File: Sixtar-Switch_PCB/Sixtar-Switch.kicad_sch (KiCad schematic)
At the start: 0 parts

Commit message: 닌텐도 스위치의 모든 버튼 및 axis 작동 확인 - GPIO0 ~ 13 = 스위치 버튼 Y, B, A, X, L트리거, R트리거, ZL트리거, ZR트리거, 마이너스, 플러스, L스틱, R스틱, 홈, 캡쳐 - GPIO14 = L스틱 왼쪽방향으로 틀기 - GPIO15 = R스틱 오른쪽방향으로 틀기
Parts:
- added K1, K10, K11, K12, K13, K14, K15, K16, K2, K3, K4, K5, K6, K7, K8, K9: KEYSW, symbol keyboard_parts:KEYSW

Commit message: kicad 회로 수정
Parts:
- added DPad_Down(GPIO17), DPad_Left(GPIO18), DPad_Right(GPIO19), DPad_Up(GPIO16): KEYSW, symbol keyboard_parts:KEYSW
- added J1: USB_C_Receptacle, symbol Connector:USB_C_Receptacle
- added R0, R1, R10, R11, R12, R13, R14, R15, R16, R17, R18, R19, R2, R3, R4, R5, R6, R7, R8, R9: 4.7k, symbol Device:R
- renumbered K10 to BT_+(GPIO9), K9 to BT_-(GPIO8), K3 to BT_A(GPIO2), K2 to BT_B(GPIO1), K14 to BT_Capture(GPIO13), K13 to BT_Home(GPIO12), K5 to BT_L(GPIO4), K11 to BT_LS(GPIO10), K15 to BT_LXAxis(GPIO14), K6 to BT_R(GPIO5), K12 to BT_RS(GPIO11), K16 to BT_RXAxis(GPIO15), K4 to BT_X(GPIO3), K1 to BT_Y(GPIO0), K7 to BT_ZL(GPIO6), K8 to BT_ZR(GPIO7)
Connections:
- net at BT_ZR(GPIO7).2: now also R7.2
- net at BT_LS(GPIO10).2: now also R10.2
- net at BT_Home(GPIO12).2: now also R12.2
- net at BT_RS(GPIO11).2: now also R11.2
- net at BT_R(GPIO5).2: now also R5.2
- net at BT_Y(GPIO0).2: now also R0.2
- net at BT_LXAxis(GPIO14).2: now also R14.2
- net at BT_Capture(GPIO13).2: now also R13.2
- net at BT_ZL(GPIO6).2: now also R6.2
- net at BT_B(GPIO1).2: now also R1.2
- net at BT_L(GPIO4).2: now also R4.2
- net at BT_A(GPIO2).2: now also R2.2
- net at BT_-(GPIO8).2: now also R8.2
- net at BT_RXAxis(GPIO15).2: now also R15.2
- net at BT_+(GPIO9).2: now also R9.2
- net at BT_X(GPIO3).2: now also R3.2
- new net: DPad_Up(GPIO16).2, R16.2
- new net: DPad_Down(GPIO17).2, R17.2
- new net: DPad_Left(GPIO18).2, R18.2
- new net: J1.A1 (GND), J1.A12 (GND), J1.B1 (GND), J1.B12 (GND)
- new net: J1.A4 (VBUS), J1.A9 (VBUS), J1.B4 (VBUS), J1.B9 (VBUS)
- new net: DPad_Right(GPIO19).2, R19.2
- no-connect marks 0 -> 10
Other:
- moved on the sheet: BT_+(GPIO9), BT_-(GPIO8), BT_A(GPIO2), BT_B(GPIO1), BT_Capture(GPIO13), BT_Home(GPIO12), BT_L(GPIO4), BT_LS(GPIO10), BT_LXAxis(GPIO14), BT_R(GPIO5), BT_RS(GPIO11), BT_RXAxis(GPIO15)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

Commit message: kicad 회로 수정
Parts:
- removed R0: 4.7k, symbol Device:R
- added C1, C2, C3: 10u, Capacitor_SMD:C_0805_2012Metric_Pad1.18x1.45mm_HandSolder, symbol Device:C
- added C10, C11, C12, C13, C5, C6, C7, C8, C9: 100u, Capacitor_SMD:C_0805_2012Metric_Pad1.18x1.45mm_HandSolder, symbol Device:C
- added C14, C15: 1u, Capacitor_SMD:C_0805_2012Metric_Pad1.18x1.45mm_HandSolder, symbol Device:C
- added C16, C17: 27p, Capacitor_SMD:C_0805_2012Metric_Pad1.18x1.45mm_HandSolder, symbol Device:C
- added C4: 100n, Capacitor_SMD:C_0805_2012Metric_Pad1.18x1.45mm_HandSolder, symbol Device:C
- added R10, R20, R9: 1k, Resistor_SMD:R_0805_2012Metric_Pad1.20x1.40mm_HandSolder, symbol Device:R
- added R2, R3: 5.1k, Resistor_SMD:R_0805_2012Metric_Pad1.20x1.40mm_HandSolder, symbol Device:R
- added R27: 4.7k, Resistor_SMD:R_0805_2012Metric_Pad1.20x1.40mm_HandSolder, symbol Device:R
- added R5, R6: 22, Resistor_SMD:R_0805_2012Metric_Pad1.20x1.40mm_HandSolder, symbol Device:R
- added SW1: USB_Boot, Connector_PinSocket_2.54mm:PinSocket_1x02_P2.54mm_Vertical, symbol Switch:SW_Push
- added SW2: RUN, Connector_PinSocket_2.54mm:PinSocket_1x02_P2.54mm_Vertical, symbol Switch:SW_Push
- added TP1, TP2: TestPoint, TestPoint:TestPoint_Pad_4.0x4.0mm, symbol Connector:TestPoint
- added U1: AMS1117-3.3, Package_TO_SOT_SMD:SOT-223-3_TabPin2, symbol Regulator_Linear:AMS1117-3.3
- added U2: W25Q128JVS, Package_SO:SOIC-8_5.23x5.23mm_P1.27mm, symbol Memory_Flash:W25Q128JVS
- added U3: RP2040, Package_DFN_QFN:QFN-56-1EP_7x7mm_P0.4mm_EP3.2x3.2mm, symbol MCU_RaspberryPi:RP2040
- added Y1: 12.000MHz(ATS,SMD), Crystal:Crystal_SMD_5032-2Pin_5.0x3.2mm, symbol Device:Crystal
- BT_+(GPIO9)1: renamed from BT_+(GPIO9); footprint (none) -> Button_Switch_Keyboard:SW_Cherry_MX_1.00u_PCB
- BT_-(GPIO8)1: renamed from BT_-(GPIO8); footprint (none) -> Button_Switch_Keyboard:SW_Cherry_MX_1.00u_PCB
- BT_A(GPIO2)1: renamed from BT_A(GPIO2); footprint (none) -> Button_Switch_Keyboard:SW_Cherry_MX_1.00u_PCB
- BT_B(GPIO1)1: renamed from BT_B(GPIO1); footprint (none) -> Button_Switch_Keyboard:SW_Cherry_MX_1.00u_PCB
- BT_Capture(GPIO13)1: renamed from BT_Capture(GPIO13); footprint (none) -> Button_Switch_Keyboard:SW_Cherry_MX_1.00u_PCB
- BT_Home(GPIO12)1: renamed from BT_Home(GPIO12); footprint (none) -> Button_Switch_Keyboard:SW_Cherry_MX_1.00u_PCB
- BT_L(GPIO4)1: renamed from BT_L(GPIO4); footprint (none) -> Button_Switch_Keyboard:SW_Cherry_MX_1.00u_PCB
- BT_LS(GPIO10)1: renamed from BT_LS(GPIO10); footprint (none) -> Button_Switch_Keyboard:SW_Cherry_MX_1.00u_PCB
- BT_LXAxis(GPIO14)1: renamed from BT_LXAxis(GPIO14); footprint (none) -> Button_Switch_Keyboard:SW_Cherry_MX_2.00u_PCB
- BT_R(GPIO5)1: renamed from BT_R(GPIO5); footprint (none) -> Button_Switch_Keyboard:SW_Cherry_MX_1.00u_PCB
- BT_RS(GPIO11)1: renamed from BT_RS(GPIO11); footprint (none) -> Button_Switch_Keyboard:SW_Cherry_MX_1.00u_PCB
- BT_RXAxis(GPIO15)1: renamed from BT_RXAxis(GPIO15); footprint (none) -> Button_Switch_Keyboard:SW_Cherry_MX_2.00u_PCB
- BT_X(GPIO3)1: renamed from BT_X(GPIO3); footprint (none) -> Button_Switch_Keyboard:SW_Cherry_MX_1.00u_PCB
- BT_Y(GPIO0)1: renamed from BT_Y(GPIO0); footprint (none) -> Button_Switch_Keyboard:SW_Cherry_MX_1.00u_PCB
- BT_ZL(GPIO6)1: renamed from BT_ZL(GPIO6); footprint (none) -> Button_Switch_Keyboard:SW_Cherry_MX_2.00u_PCB
- BT_ZR(GPIO7)1: renamed from BT_ZR(GPIO7); footprint (none) -> Button_Switch_Keyboard:SW_Cherry_MX_2.00u_PCB
- DPad_Down(GPIO17)1: renamed from DPad_Down(GPIO17); footprint (none) -> Button_Switch_Keyboard:SW_Cherry_MX_1.00u_PCB
- DPad_Left(GPIO18)1: renamed from DPad_Left(GPIO18); footprint (none) -> Button_Switch_Keyboard:SW_Cherry_MX_1.00u_PCB
- DPad_Right(GPIO19)1: renamed from DPad_Right(GPIO19); footprint (none) -> Button_Switch_Keyboard:SW_Cherry_MX_1.00u_PCB
- DPad_Up(GPIO16)1: renamed from DPad_Up(GPIO16); footprint (none) -> Button_Switch_Keyboard:SW_Cherry_MX_1.00u_PCB
- J1: footprint (none) -> Connector_USB:USB_C_Receptacle_XKB_U262-16XN-4BVC11
- R1: footprint (none) -> Resistor_SMD:R_0805_2012Metric_Pad1.20x1.40mm_HandSolder
- R11: renamed from R5; footprint (none) -> Resistor_SMD:R_0805_2012Metric_Pad1.20x1.40mm_HandSolder
- R12: renamed from R6; footprint (none) -> Resistor_SMD:R_0805_2012Metric_Pad1.20x1.40mm_HandSolder
- R13: renamed from R7; footprint (none) -> Resistor_SMD:R_0805_2012Metric_Pad1.20x1.40mm_HandSolder
- R14: renamed from R8; footprint (none) -> Resistor_SMD:R_0805_2012Metric_Pad1.20x1.40mm_HandSolder
- R15: renamed from R9; footprint (none) -> Resistor_SMD:R_0805_2012Metric_Pad1.20x1.40mm_HandSolder
- R16: renamed from R10; footprint (none) -> Resistor_SMD:R_0805_2012Metric_Pad1.20x1.40mm_HandSolder
- R17: renamed from R11; footprint (none) -> Resistor_SMD:R_0805_2012Metric_Pad1.20x1.40mm_HandSolder
- R18: renamed from R12; footprint (none) -> Resistor_SMD:R_0805_2012Metric_Pad1.20x1.40mm_HandSolder
- R19: renamed from R13; footprint (none) -> Resistor_SMD:R_0805_2012Metric_Pad1.20x1.40mm_HandSolder
- R21: renamed from R14; footprint (none) -> Resistor_SMD:R_0805_2012Metric_Pad1.20x1.40mm_HandSolder
- R22: renamed from R15; footprint (none) -> Resistor_SMD:R_0805_2012Metric_Pad1.20x1.40mm_HandSolder
- R23: renamed from R16; footprint (none) -> Resistor_SMD:R_0805_2012Metric_Pad1.20x1.40mm_HandSolder
- R24: renamed from R17; footprint (none) -> Resistor_SMD:R_0805_2012Metric_Pad1.20x1.40mm_HandSolder
- R25: renamed from R18; footprint (none) -> Resistor_SMD:R_0805_2012Metric_Pad1.20x1.40mm_HandSolder
- R26: renamed from R19; footprint (none) -> Resistor_SMD:R_0805_2012Metric_Pad1.20x1.40mm_HandSolder
- R4: renamed from R2; footprint (none) -> Resistor_SMD:R_0805_2012Metric_Pad1.20x1.40mm_HandSolder
- R7: renamed from R3; footprint (none) -> Resistor_SMD:R_0805_2012Metric_Pad1.20x1.40mm_HandSolder
- R8: renamed from R4; footprint (none) -> Resistor_SMD:R_0805_2012Metric_Pad1.20x1.40mm_HandSolder
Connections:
- net GND: now reaches BT_ZR(GPIO7)1.1
- net GND: now also BT_+(GPIO9)1.1, BT_-(GPIO8)1.1, BT_A(GPIO2)1.1, BT_B(GPIO1)1.1, BT_Capture(GPIO13)1.1, BT_Home(GPIO12)1.1, BT_L(GPIO4)1.1, BT_LS(GPIO10)1.1, BT_LXAxis(GPIO14)1.1, BT_R(GPIO5)1.1, BT_RS(GPIO11)1.1, BT_RXAxis(GPIO15)1.1, BT_X(GPIO3)1.1, BT_Y(GPIO0)1.1, BT_ZL(GPIO6)1.1, DPad_Down(GPIO17)1.1, DPad_Left(GPIO18)1.1, DPad_Right(GPIO19)1.1, DPad_Up(GPIO16)1.1, J1.A1 (GND), J1.A12 (GND), J1.B1 (GND), J1.B12 (GND), C1.1, C10.2, C11.2, C12.2, C13.2, C14.2, C15.2, C16.1, C17.1, C2.1, C3.1, C4.2, C5.2, C6.2, C7.2, C8.2, C9.2, R2.2, R3.2, SW1.1, SW2.1, U1.1 (GND), U2.4 (GND), U3.19 (TESTEN), U3.57 (GND)
- net BTN_ZL: now reaches R13.2
- net BTN_ZL: now also BT_ZL(GPIO6)1.2, U3.8 (GPIO6); no longer BT_ZR(GPIO7)1.2
- net +3.3V: now reaches R11.1
- net +3.3V: now also R1.1, R12.1, R13.1, R14.1, R15.1, R16.1, R17.1, R18.1, R19.1, R21.1, R22.1, R23.1, R24.1, R25.1, R26.1, R4.1, R7.1, R8.1, C10.1, C11.1, C12.1, C13.1, C15.1, C2.2, C3.2, C4.1, C7.1, C8.1, C9.1, R27.1, R9.2, U1.2 (VO), U2.8 (VCC), U3.1 (IOVDD), U3.10 (IOVDD), U3.22 (IOVDD), U3.33 (IOVDD), U3.42 (IOVDD), U3.43 (ADC_AVDD), U3.44 (VREG_IN), U3.48 (USB_VDD), U3.49 (IOVDD)
- net BTN_L: now reaches R11.2
- net BTN_L: now also BT_L(GPIO4)1.2, U3.6 (GPIO4); no longer BT_R(GPIO5)1.2
- net BTN_RXAxis: now reaches R23.2
- net BTN_RXAxis: now also BT_RXAxis(GPIO15)1.2, U3.18 (GPIO15); no longer DPad_Up(GPIO16)1.2
- net BTN_Capture: now reaches BT_Capture(GPIO13)1.2
- net BTN_Capture: now also R21.2, U3.16 (GPIO13); no longer R19.2
- net DPad_Down: now reaches DPad_Down(GPIO17)1.2
- net DPad_Down: now also R25.2, U3.28 (GPIO17); no longer R24.2
- net BTN_LS: now reaches BT_LS(GPIO10)1.2
- net BTN_LS: now also R17.2, U3.13 (GPIO10); no longer R16.2
- net BTN_B: now reaches BT_B(GPIO1)1.2
- net BTN_B: now also R4.2, U3.3 (GPIO1); no longer R1.2
- net BTN_Home: now reaches BT_Home(GPIO12)1.2
- net BTN_Home: now also R19.2, U3.15 (GPIO12); no longer R18.2
- net BTN_RS: now reaches BT_RS(GPIO11)1.2
- net BTN_RS: now also R18.2, U3.14 (GPIO11); no longer R17.2
- net DPad_Left: now reaches DPad_Left(GPIO18)1.2
- net DPad_Left: now also R26.2, U3.29 (GPIO18); no longer R25.2
- net BTN_Y: now reaches BT_Y(GPIO0)1.2
- net BTN_Y: now also R1.2, U3.2 (GPIO0)
- net BTN_LXAxis: now reaches BT_LXAxis(GPIO14)1.2
- net BTN_LXAxis: now also R22.2, U3.17 (GPIO14); no longer R21.2
- net BTN_Minus: now reaches R15.2
- net BTN_Minus: now also BT_-(GPIO8)1.2, U3.11 (GPIO8); no longer BT_+(GPIO9)1.2
- net BTN_R: now reaches R12.2
- net BTN_R: now also BT_R(GPIO5)1.2, U3.7 (GPIO5); no longer BT_ZL(GPIO6)1.2
- net VBUS: now reaches J1.A4 (VBUS), J1.A9 (VBUS), J1.B4 (VBUS), J1.B9 (VBUS)
- net VBUS: now also C1.2, U1.3 (VI)
- net at J1.A5 (CC1): now also R2.1
- net D+: now reaches J1.A6 (D+)
- net D+: now also J1.B6 (D+), R6.1
- net D-: now reaches J1.A7 (D-)
- net D-: now also J1.B7 (D-), R5.1
- net at J1.B5 (CC2): now also R3.1
- net GNDPWR: now reaches J1.S1 (SHIELD)
- net BTN_X: now reaches R8.2
- net BTN_X: now also BT_X(GPIO3)1.2, U3.5 (GPIO3); no longer BT_L(GPIO4)1.2
- net BTN_A: now reaches BT_A(GPIO2)1.2
- net BTN_A: now also R7.2, U3.4 (GPIO2); no longer R4.2
- net BTN_ZR: now reaches R14.2
- net BTN_ZR: now also BT_ZR(GPIO7)1.2, U3.9 (GPIO7); no longer BT_-(GPIO8)1.2
- net DPad_Right: now reaches DPad_Right(GPIO19)1.2
- net DPad_Right: now also R27.2, U3.30 (GPIO19); no longer R26.2
- new net: C17.2, R20.1, Y1.1
- new net: C16.2, U3.20 (XIN), Y1.2
- new net: R20.2, U3.21 (XOUT)
- new net: TP1.1, U3.24 (SWCLK)
- new net: TP2.1, U3.25 (SWD)
- new net: SW2.2, U3.26 (RUN)
- new net: R10.1, SW1.2
- new net +1V1: C14.1, C5.1, C6.1, U3.23 (DVDD), U3.45 (VREG_VOUT), U3.50 (DVDD)
- new net BTN_Plus: BT_+(GPIO9)1.2, R16.2, U3.12 (GPIO9)
- new net DPad_Up: DPad_Up(GPIO16)1.2, R24.2, U3.27 (GPIO16)
- new net QSPI_SCLK: U2.6 (CLK), U3.52 (QSPI_SCLK)
- new net QSPI_SD0: U2.5 (DI(IO0)), U3.53 (QSPI_SD0)
- new net QSPI_SD1: U2.2 (DO(IO1)), U3.55 (QSPI_SD1)
- new net QSPI_SD2: U2.3 (IO2), U3.54 (QSPI_SD2)
- new net QSPI_SD3: U2.7 (IO3), U3.51 (QSPI_SD3)
- new net QSPI_SS: R10.2, R9.1, U2.1 (~{CS}), U3.56 (QSPI_SS)
- new net RP_D+: R6.2, U3.47 (USB_DP)
- new net RP_D-: R5.2, U3.46 (USB_DM)
- no-connect marks 10 -> 20
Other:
- moved on the sheet: BT_+(GPIO9)1, BT_-(GPIO8)1, BT_A(GPIO2)1, BT_B(GPIO1)1, BT_Capture(GPIO13)1, BT_Home(GPIO12)1, BT_L(GPIO4)1, BT_LS(GPIO10)1, BT_LXAxis(GPIO14)1, BT_R(GPIO5)1, BT_RS(GPIO11)1, BT_RXAxis(GPIO15)1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

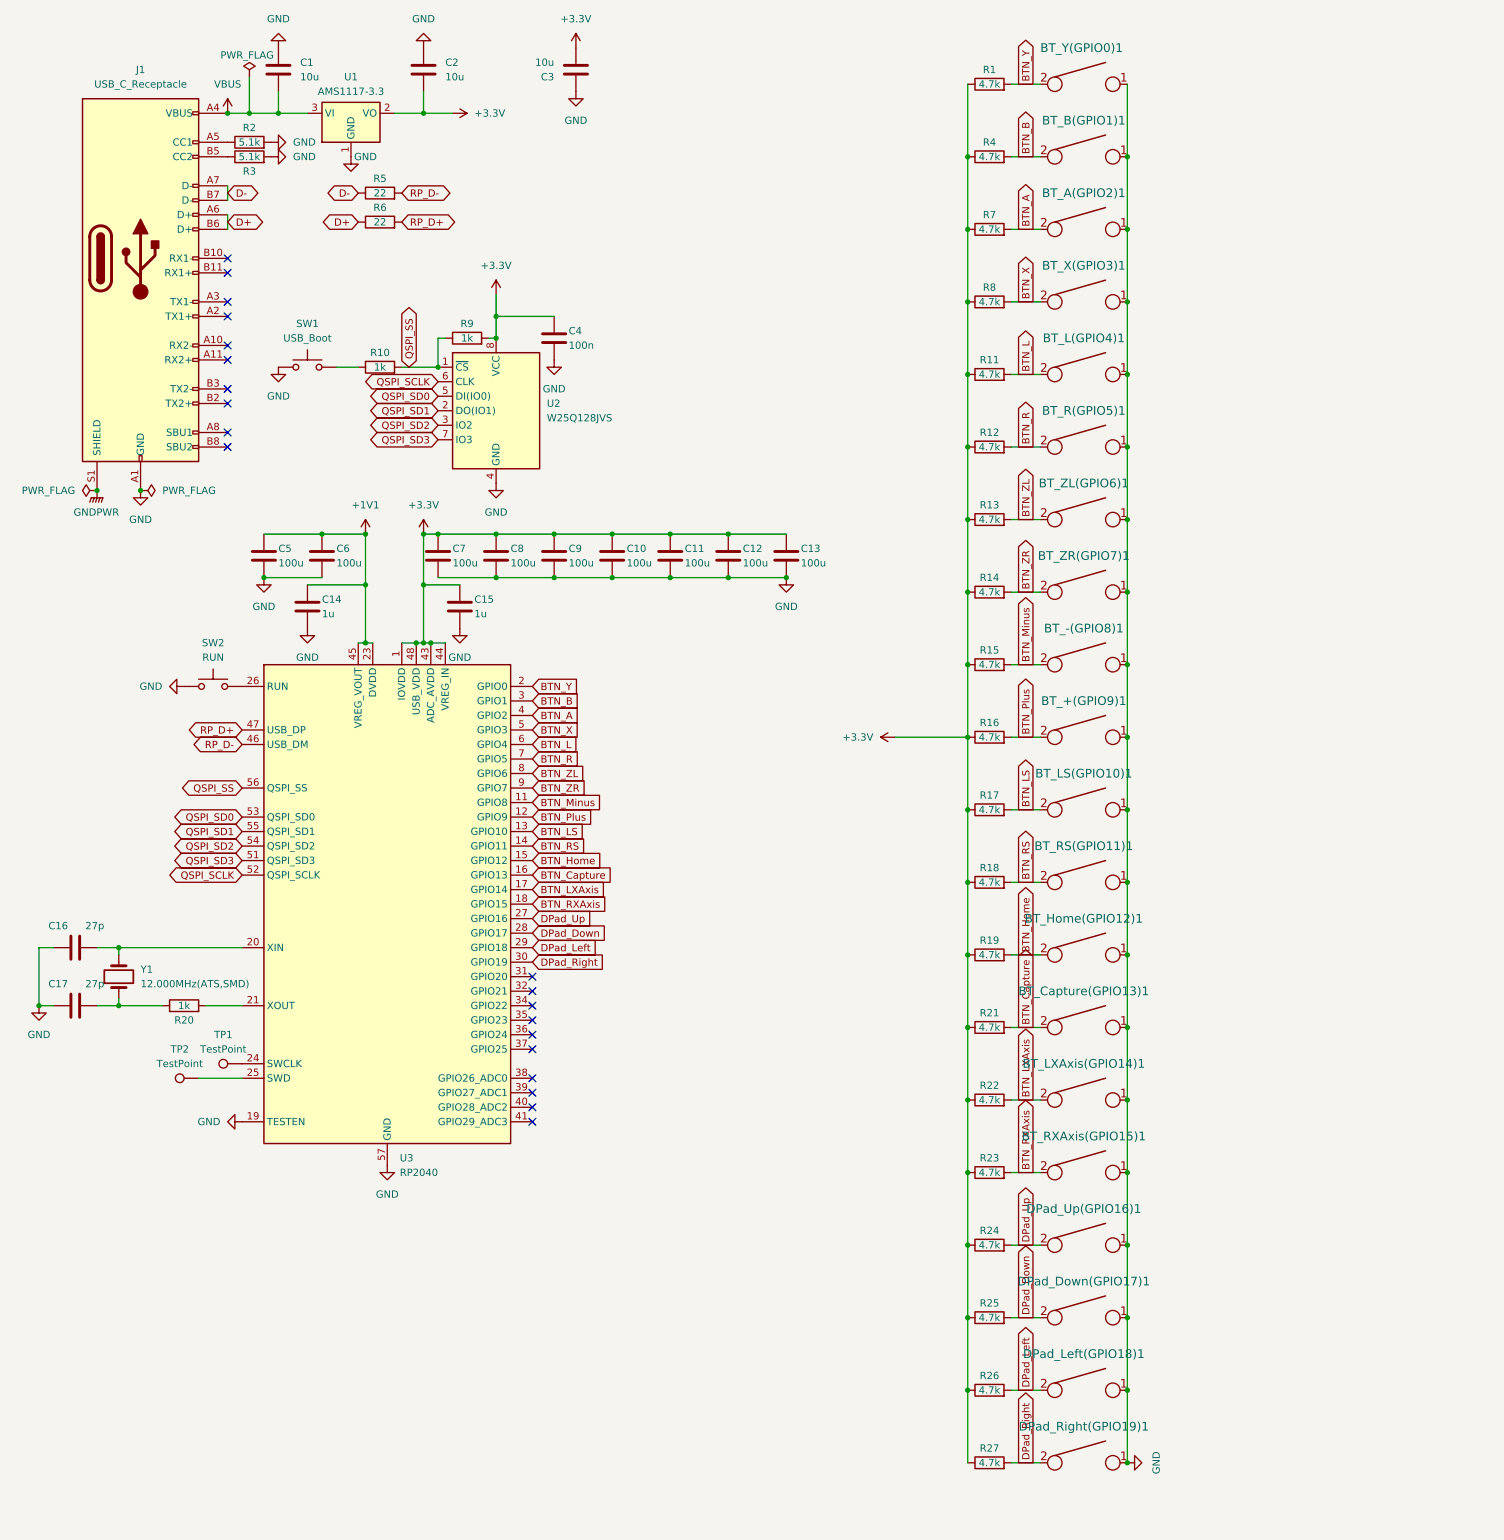
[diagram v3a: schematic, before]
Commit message: KiCAD 회로 수정 및 PCB 제작중
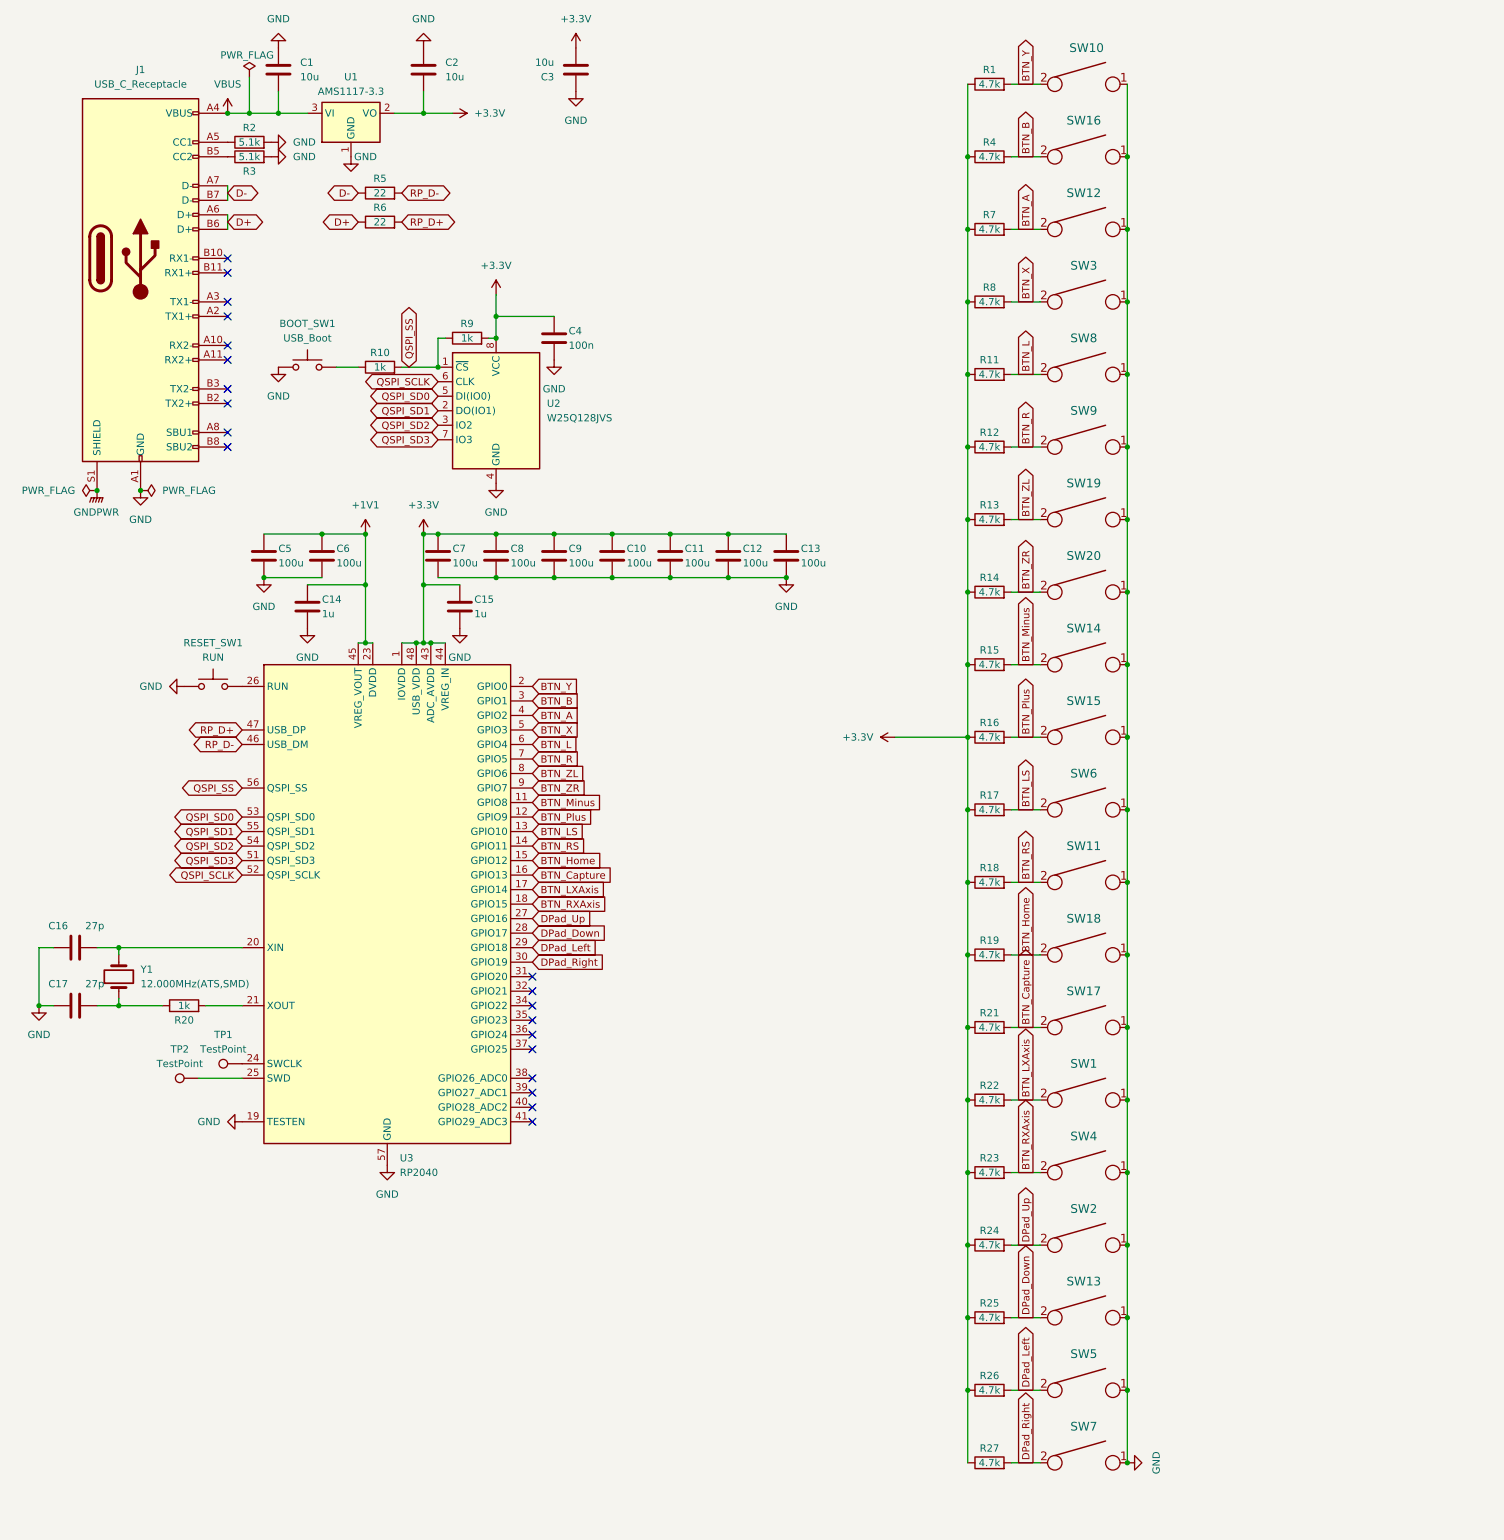
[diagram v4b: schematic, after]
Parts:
- renumbered SW1 to BOOT_SW1, SW2 to RESET_SW1, BT_LXAxis(GPIO14)1 to SW1, BT_Y(GPIO0)1 to SW10, BT_RS(GPIO11)1 to SW11, BT_A(GPIO2)1 to SW12, DPad_Down(GPIO17)1 to SW13, BT_-(GPIO8)1 to SW14, BT_+(GPIO9)1 to SW15, BT_B(GPIO1)1 to SW16, BT_Capture(GPIO13)1 to SW17, BT_Home(GPIO12)1 to SW18, BT_ZL(GPIO6)1 to SW19, DPad_Up(GPIO16)1 to SW2, BT_ZR(GPIO7)1 to SW20, BT_X(GPIO3)1 to SW3, BT_RXAxis(GPIO15)1 to SW4, DPad_Left(GPIO18)1 to SW5, BT_LS(GPIO10)1 to SW6, DPad_Right(GPIO19)1 to SW7, BT_L(GPIO4)1 to SW8, BT_R(GPIO5)1 to SW9

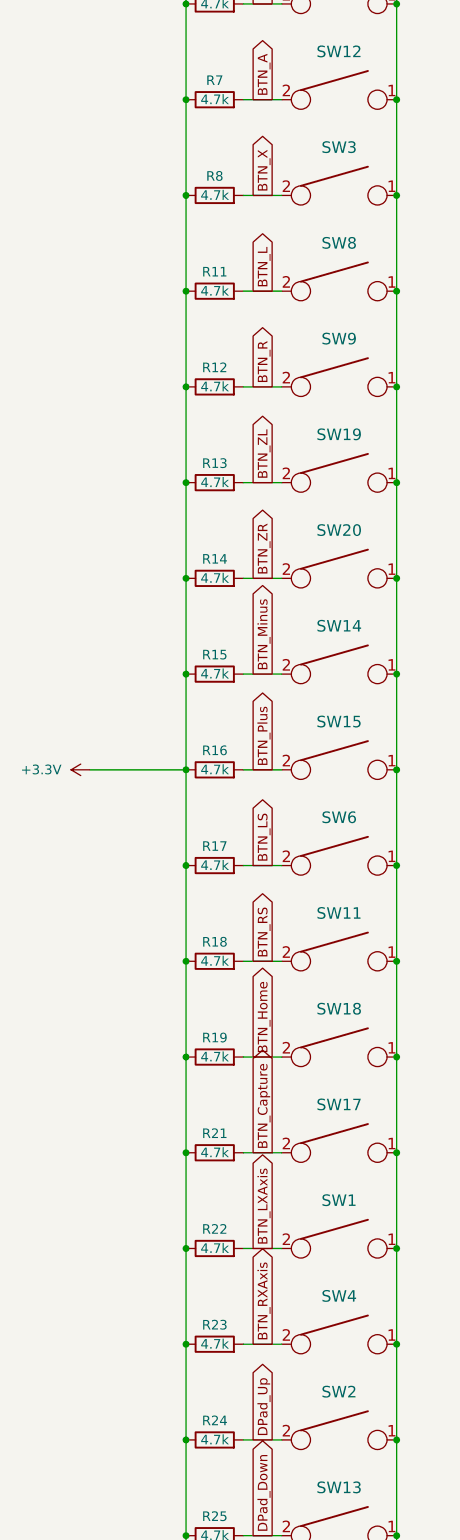
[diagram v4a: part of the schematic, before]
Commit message: 키 배치 수정
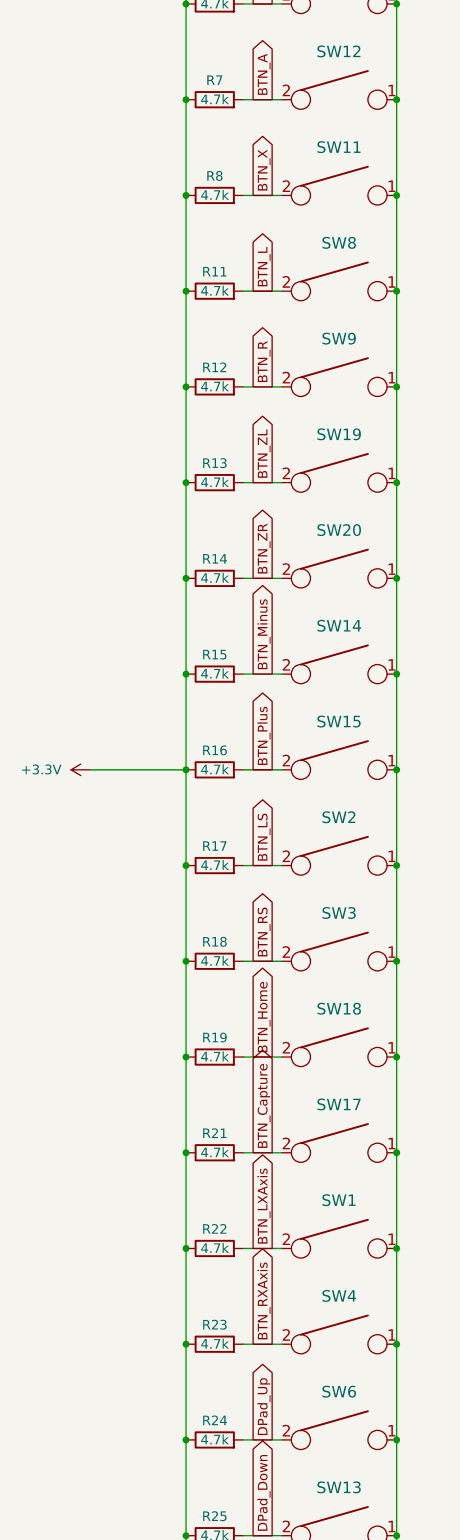
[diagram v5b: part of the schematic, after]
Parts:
- renumbered SW3 to SW11, SW6 to SW2, SW11 to SW3, SW2 to SW6
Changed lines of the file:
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@@
   (symbol (lib_id "keyboard_parts:KEYSW") (at 198.12 152.4 0) (unit 1)
     (in_bom yes) (on_board yes) (dnp no) (fields_autoplaced)
-    (property "Reference" "SW6" (at 198.12 146.05 0)
+    (property "Reference" "SW2" (at 198.12 146.05 0)
       (effects (font (size 1.524 1.524)))
     )
@@
       (project "Sixtar-Switch"
         (path "/c7d20cc9-129e-4a64-9aac-b63eeee7ae8b"
-          (reference "SW6") (unit 1)
+          (reference "SW2") (unit 1)
         )
       )
@@
   (symbol (lib_id "keyboard_parts:KEYSW") (at 198.12 165.1 0) (unit 1)
     (in_bom yes) (on_board yes) (dnp no) (fields_autoplaced)
-    (property "Reference" "SW11" (at 198.12 158.75 0)
+    (property "Reference" "SW3" (at 198.12 158.75 0)
       (effects (font (size 1.524 1.524)))
     )
@@
       (project "Sixtar-Switch"
         (path "/c7d20cc9-129e-4a64-9aac-b63eeee7ae8b"
-          (reference "SW11") (unit 1)
+          (reference "SW3") (unit 1)
         )
       )
@@
   (symbol (lib_id "keyboard_parts:KEYSW") (at 198.12 63.5 0) (unit 1)
     (in_bom yes) (on_board yes) (dnp no) (fields_autoplaced)
-    (property "Reference" "SW3" (at 198.12 57.15 0)
+    (property "Reference" "SW11" (at 198.12 57.15 0)
       (effects (font (size 1.524 1.524)))
     )
@@
       (project "Sixtar-Switch"
         (path "/c7d20cc9-129e-4a64-9aac-b63eeee7ae8b"
-          (reference "SW3") (unit 1)
+          (reference "SW11") (unit 1)
         )
       )
@@
   (symbol (lib_id "keyboard_parts:KEYSW") (at 198.12 228.6 0) (unit 1)
     (in_bom yes) (on_board yes) (dnp no) (fields_autoplaced)
-    (property "Reference" "SW2" (at 198.12 222.25 0)
+    (property "Reference" "SW6" (at 198.12 222.25 0)
       (effects (font (size 1.524 1.524)))
     )
@@
       (project "Sixtar-Switch"
         (path "/c7d20cc9-129e-4a64-9aac-b63eeee7ae8b"
-          (reference "SW2") (unit 1)
-        )
-      )
+          (reference "SW6") (unit 1)
+        )
+      )

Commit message: PCB빌드 완료. 테스트 필요
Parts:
- removed TP1, TP2: TestPoint, TestPoint:TestPoint_Pad_4.0x4.0mm, symbol Connector:TestPoint
- added H1, H2, H3, H4: MountingHole, MountingHole:MountingHole_3.2mm_M3, symbol Mechanical:MountingHole
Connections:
- no-connect marks 20 -> 22
